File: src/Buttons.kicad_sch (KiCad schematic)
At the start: 23 parts

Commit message: Update Schematics design
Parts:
- renumbered JP4 to JP1, JP5 to JP2, JP6 to JP3
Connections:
- net +BATT: now also SW?.1 (A); no longer SW?.3 (C)
- net GND: now also SW?.3 (C); no longer SW?.1 (A)
- net GND1 renamed GNDDash
- net GND2 renamed GNDEBlinker

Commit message: update Schematics
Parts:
- removed D? (x2): LED, LED_THT:LED_D5.0mm, symbol Device:LED
- removed J? (x4): MiniFit_2x03_F, Connector_Molex:Molex_Mini-Fit_Jr_5566-06A_2x03_P4.20mm_Vertical, symbol Connector_Generic:Conn_02x03_Counter_Clockwise
- removed JP1, JP2, JP3: Jumper_3_Bridged12, symbol Jumper:Jumper_3_Bridged12
- removed R? (x2): 470R, Resistor_THT:R_Axial_DIN0204_L3.6mm_D1.6mm_P5.08mm_Horizontal, symbol Device:R
- removed SW? (x2): SW_SPDT, symbol Switch:SW_SPDT
- added D?: LED, LED_THT:LED_D5.0mm, symbol Device:LED
- added J? (x3): MiniFit_2x03_F, Connector_Molex:Molex_Mini-Fit_Jr_5566-06A_2x03_P4.20mm_Vertical, symbol Connector_Generic:Conn_02x03_Counter_Clockwise
- added JP1: Jumper_3_Open, symbol Jumper:Jumper_3_Open
- added R?: 470R, Resistor_THT:R_Axial_DIN0204_L3.6mm_D1.6mm_P5.08mm_Horizontal, symbol Device:R
- added SW?: SW_SPDT, symbol Switch:SW_SPDT
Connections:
- net +5V: now also J?.3 (Pin_3), JP1.3 (B)
- net +BATT: now also J?.1 (Pin_1), R?.2
- net Accessory: now also R?.2, J?.1 (Pin_1), J?.4 (Pin_4)
- net GND: now also J?.2 (Pin_2), J?.2 (Pin_2), J?.2 (Pin_2), SW?.1 (A)
- net GNDDash: now also D?.1 (K), J?.5 (Pin_5), J?.5 (Pin_5), J?.5 (Pin_5)
- net VInst: now also J?.1 (Pin_1), J?.1 (Pin_1), J?.6 (Pin_6), JP1.1 (A), R?.2; no longer J?.1 (Pin_1), R?.2, R?.2
- net VLight: now also SW?.3 (C), J?.3 (Pin_3)
- net at SW?.3 (C): now also JP1.2 (C)
- net AuxSwitch1 renamed AuxSwitch
- net AuxSwitch: now also J?.4 (Pin_4)
- net BSignal renamed SignalRelay
- net EBlinker renamed Hazard
- net GNDEBlinker renamed HazardLed
- new net: D?.2 (A), R?.1
- new net VOutlet: J?.3 (Pin_3), SW?.3 (C)
- new net VOutlet_Jack: J?.4 (Pin_4), SW?.2 (B)
- no-connect marks 2 -> 3
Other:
- note added: "Auxiliary Beams Buttons"
- note added: "DC Outlet Button"
- note removed: "Auxiliary Beam Buttons"
- note removed: "Kill switch button"
- moved on the sheet: D?, R?, SW?

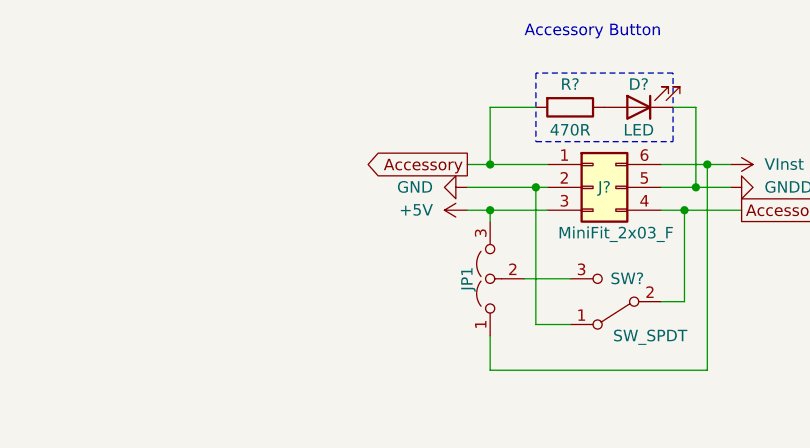
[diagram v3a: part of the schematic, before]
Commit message: Update Schmatics; Cleanup unecessary circuits; Simplify blinkers dimmers; Update PCB; Colorize motorcycle electric diagram.
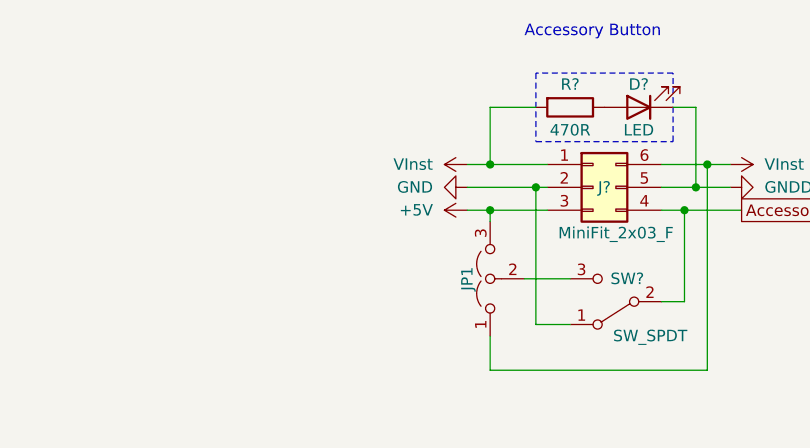
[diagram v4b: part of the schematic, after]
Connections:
- net Accessory: no longer J?.1 (Pin_1), R?.2
- net VInst: now also J?.1 (Pin_1), R?.2
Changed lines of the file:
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@@
-    )
-  )
-  (global_label "Accessory" (shape output) (at 189.23 52.07 180) (fields_autoplaced)
-    (effects (font (size 1.27 1.27)) (justify right))
-    (property "Intersheetrefs" "${INTERSHEET_REFS}" (at 177.0108 52.07 0)
-      (effects (font (size 1.27 1.27)) (justify right) hide)
     )
   )
@@
         )
         (path "/e63e39d7-6ac0-4ffd-8aa3-1841a4541b55/d73eba3b-b563-44cf-9a80-01658b690b2a"
-          (reference "J5") (unit 1)
+          (reference "J42") (unit 1)
         )
       )
@@
         )
         (path "/e63e39d7-6ac0-4ffd-8aa3-1841a4541b55/d73eba3b-b563-44cf-9a80-01658b690b2a"
-          (reference "#PWR045") (unit 1)
+          (reference "#PWR060") (unit 1)
         )
       )
@@
         )
         (path "/e63e39d7-6ac0-4ffd-8aa3-1841a4541b55/d73eba3b-b563-44cf-9a80-01658b690b2a"
-          (reference "D14") (unit 1)
+          (reference "D16") (unit 1)
         )
       )
@@
         )
         (path "/e63e39d7-6ac0-4ffd-8aa3-1841a4541b55/d73eba3b-b563-44cf-9a80-01658b690b2a"
-          (reference "#PWR050") (unit 1)
+          (reference "#PWR062") (unit 1)
         )
       )
@@
         )
         (path "/e63e39d7-6ac0-4ffd-8aa3-1841a4541b55/d73eba3b-b563-44cf-9a80-01658b690b2a"
-          (reference "#PWR040") (unit 1)
+          (reference "#PWR058") (unit 1)
         )
       )
@@
         )
         (path "/e63e39d7-6ac0-4ffd-8aa3-1841a4541b55/d73eba3b-b563-44cf-9a80-01658b690b2a"
-          (reference "J7") (unit 1)
+          (reference "J41") (unit 1)
         )
       )
@@
         )
         (path "/e63e39d7-6ac0-4ffd-8aa3-1841a4541b55/d73eba3b-b563-44cf-9a80-01658b690b2a"
-          (reference "J4") (unit 1)
+          (reference "J43") (unit 1)
+        )
+      )
+    )
+  )
+  (symbol (lib_name "VInst_2") (lib_id "Local Components:VInst") (at 189.23 52.07 90) (unit 1)
+    (in_bom yes) (on_board yes) (dnp no)
+    (property "Reference" "#PWR?" (at 189.23 48.26 0)
+      (effects (font (size 1.27 1.27)) hide)
+    )
+    (property "Value" "VInst" (at 185.42 52.07 90)
+      (effects (font (size 1.27 1.27)) (justify left))
+    )
+    (property "Footprint" "" (at 189.23 52.07 0)
+      (effects (font (size 1.27 1.27)) hide)
+    )
+    (property "Datasheet" "" (at 189.23 52.07 0)
+      (effects (font (size 1.27 1.27)) hide)
+    )
+    (pin "1")
+    (instances
+      (project "dragstar-infotainment"
+        (path "/e63e39d7-6ac0-4ffd-8aa3-1841a4541b55"
+          (reference "#PWR?") (unit 1)
+        )
+        (path "/e63e39d7-6ac0-4ffd-8aa3-1841a4541b55/d73eba3b-b563-44cf-9a80-01658b690b2a"
+          (reference "#PWR057") (unit 1)
         )
       )
@@
         )
         (path "/e63e39d7-6ac0-4ffd-8aa3-1841a4541b55/d73eba3b-b563-44cf-9a80-01658b690b2a"
-          (reference "J6") (unit 1)
+          (reference "J44") (unit 1)
         )
       )
@@
         )
         (path "/e63e39d7-6ac0-4ffd-8aa3-1841a4541b55/d73eba3b-b563-44cf-9a80-01658b690b2a"
-          (reference "#PWR046") (unit 1)
+          (reference "#PWR061") (unit 1)
         )
       )
@@
         )
         (path "/e63e39d7-6ac0-4ffd-8aa3-1841a4541b55/d73eba3b-b563-44cf-9a80-01658b690b2a"
-          (reference "SW1") (unit 1)
+          (reference "SW3") (unit 1)
         )
       )
@@
         )
         (path "/e63e39d7-6ac0-4ffd-8aa3-1841a4541b55/d73eba3b-b563-44cf-9a80-01658b690b2a"
-          (reference "#PWR041") (unit 1)
+          (reference "#PWR065") (unit 1)
         )
       )
@@
         )
         (path "/e63e39d7-6ac0-4ffd-8aa3-1841a4541b55/d73eba3b-b563-44cf-9a80-01658b690b2a"
-          (reference "#PWR053") (unit 1)
+          (reference "#PWR056") (unit 1)
         )
       )
@@
         )
         (path "/e63e39d7-6ac0-4ffd-8aa3-1841a4541b55/d73eba3b-b563-44cf-9a80-01658b690b2a"
-          (reference "#PWR044") (unit 1)
+          (reference "#PWR054") (unit 1)
         )
       )
@@
         )
         (path "/e63e39d7-6ac0-4ffd-8aa3-1841a4541b55/d73eba3b-b563-44cf-9a80-01658b690b2a"
-          (reference "D16") (unit 1)
+          (reference "D15") (unit 1)
         )
       )
@@
         )
         (path "/e63e39d7-6ac0-4ffd-8aa3-1841a4541b55/d73eba3b-b563-44cf-9a80-01658b690b2a"
-          (reference "R7") (unit 1)
+          (reference "R11") (unit 1)
         )
       )
@@
         )
         (path "/e63e39d7-6ac0-4ffd-8aa3-1841a4541b55/d73eba3b-b563-44cf-9a80-01658b690b2a"
-          (reference "#PWR049") (unit 1)
+          (reference "#PWR055") (unit 1)
         )
       )
@@
         )
         (path "/e63e39d7-6ac0-4ffd-8aa3-1841a4541b55/d73eba3b-b563-44cf-9a80-01658b690b2a"
-          (reference "R8") (unit 1)
+          (reference "R10") (unit 1)
         )
       )
@@
         )
         (path "/e63e39d7-6ac0-4ffd-8aa3-1841a4541b55/d73eba3b-b563-44cf-9a80-01658b690b2a"
-          (reference "D15") (unit 1)
+          (reference "D18") (unit 1)
         )
       )
@@
         )
         (path "/e63e39d7-6ac0-4ffd-8aa3-1841a4541b55/d73eba3b-b563-44cf-9a80-01658b690b2a"
-          (reference "#PWR039") (unit 1)
+          (reference "#PWR064") (unit 1)
         )
       )
@@
         )
         (path "/e63e39d7-6ac0-4ffd-8aa3-1841a4541b55/d73eba3b-b563-44cf-9a80-01658b690b2a"
-          (reference "#PWR047") (unit 1)
+          (reference "#PWR063") (unit 1)
         )
       )
@@
         )
         (path "/e63e39d7-6ac0-4ffd-8aa3-1841a4541b55/d73eba3b-b563-44cf-9a80-01658b690b2a"
-          (reference "R9") (unit 1)
+          (reference "R12") (unit 1)
         )
       )
@@
         )
         (path "/e63e39d7-6ac0-4ffd-8aa3-1841a4541b55/d73eba3b-b563-44cf-9a80-01658b690b2a"
-          (reference "D13") (unit 1)
+          (reference "D17") (unit 1)
         )
       )
@@
         )
         (path "/e63e39d7-6ac0-4ffd-8aa3-1841a4541b55/d73eba3b-b563-44cf-9a80-01658b690b2a"
-          (reference "#PWR042") (unit 1)
+          (reference "#PWR059") (unit 1)
         )
       )
@@
         )
         (path "/e63e39d7-6ac0-4ffd-8aa3-1841a4541b55/d73eba3b-b563-44cf-9a80-01658b690b2a"
-          (reference "#PWR048") (unit 1)
+          (reference "#PWR050") (unit 1)
         )
       )
@@
         )
         (path "/e63e39d7-6ac0-4ffd-8aa3-1841a4541b55/5d40715c-dfc9-4b95-9cc7-adbd4b609d9b"
-          (reference "#PWR027") (unit 1)
+          (reference "#PWR?") (unit 1)
         )
         (path "/e63e39d7-6ac0-4ffd-8aa3-1841a4541b55/5d40715c-dfc9-4b95-9cc7-adbd4b609d9b/cd89aa2b-c893-42fb-9925-ff5352d2269d"
-          (reference "#PWR0105") (unit 1)
-        )
-        (path "/e63e39d7-6ac0-4ffd-8aa3-1841a4541b55/d73eba3b-b563-44cf-9a80-01658b690b2a"
-          (reference "#PWR038") (unit 1)
+          (reference "#PWR?") (unit 1)
+        )
+        (path "/e63e39d7-6ac0-4ffd-8aa3-1841a4541b55/d73eba3b-b563-44cf-9a80-01658b690b2a"
+          (reference "#PWR053") (unit 1)
         )
       )
@@
         )
         (path "/e63e39d7-6ac0-4ffd-8aa3-1841a4541b55/d73eba3b-b563-44cf-9a80-01658b690b2a"
-          (reference "SW3") (unit 1)
+          (reference "SW4") (unit 1)
         )
       )
@@
         )
         (path "/e63e39d7-6ac0-4ffd-8aa3-1841a4541b55/d73eba3b-b563-44cf-9a80-01658b690b2a"
-          (reference "R10") (unit 1)
+          (reference "R9") (unit 1)
         )
       )
@@
         )
         (path "/e63e39d7-6ac0-4ffd-8aa3-1841a4541b55/d73eba3b-b563-44cf-9a80-01658b690b2a"
-          (reference "SW4") (unit 1)
-        )
-      )
+          (reference "SW1") (unit 1)
+        )
+      )

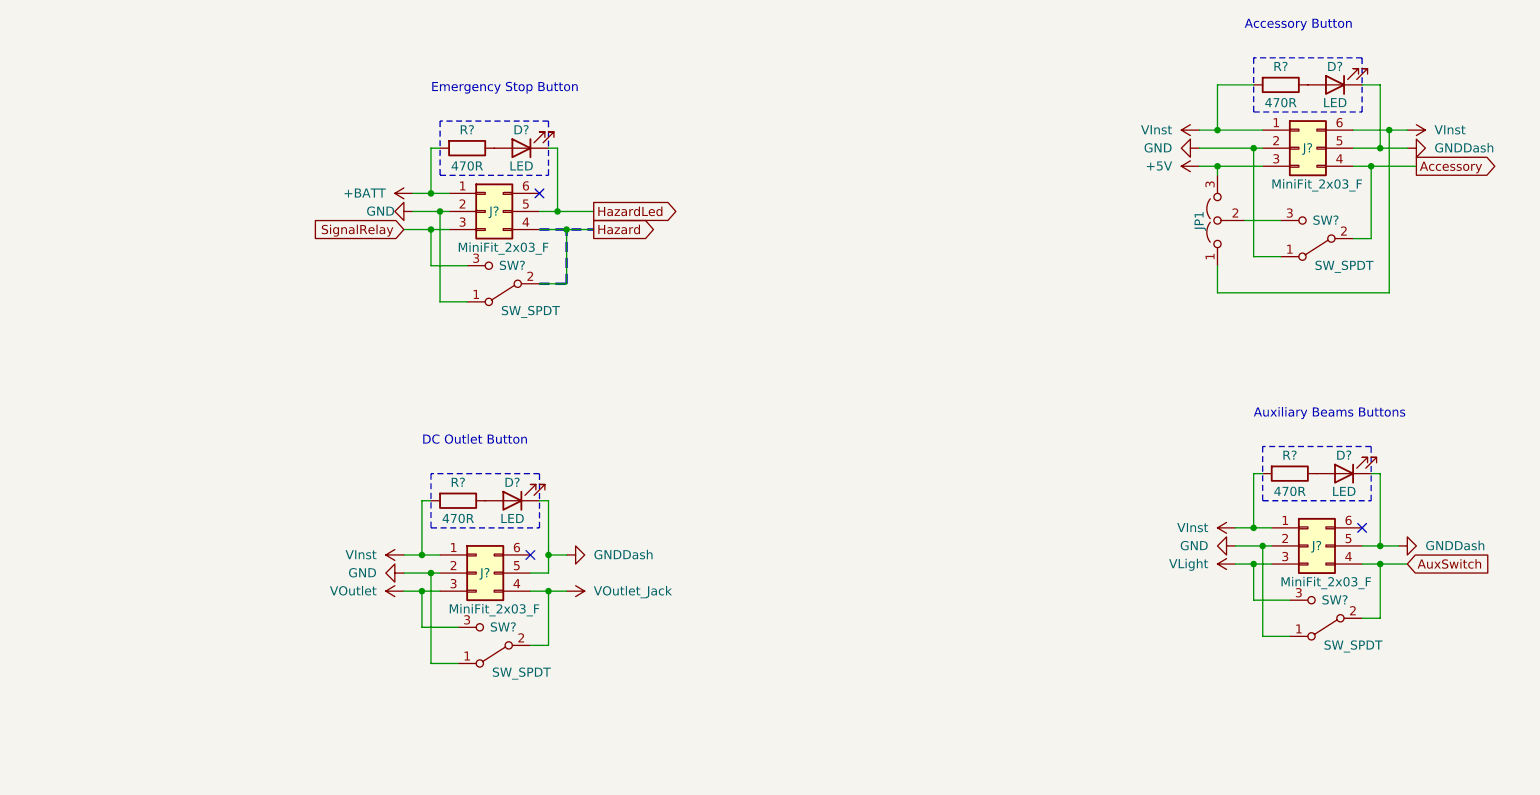
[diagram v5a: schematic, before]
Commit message: simplify circuit diagram. Remove unecessary features; Split board into two components|
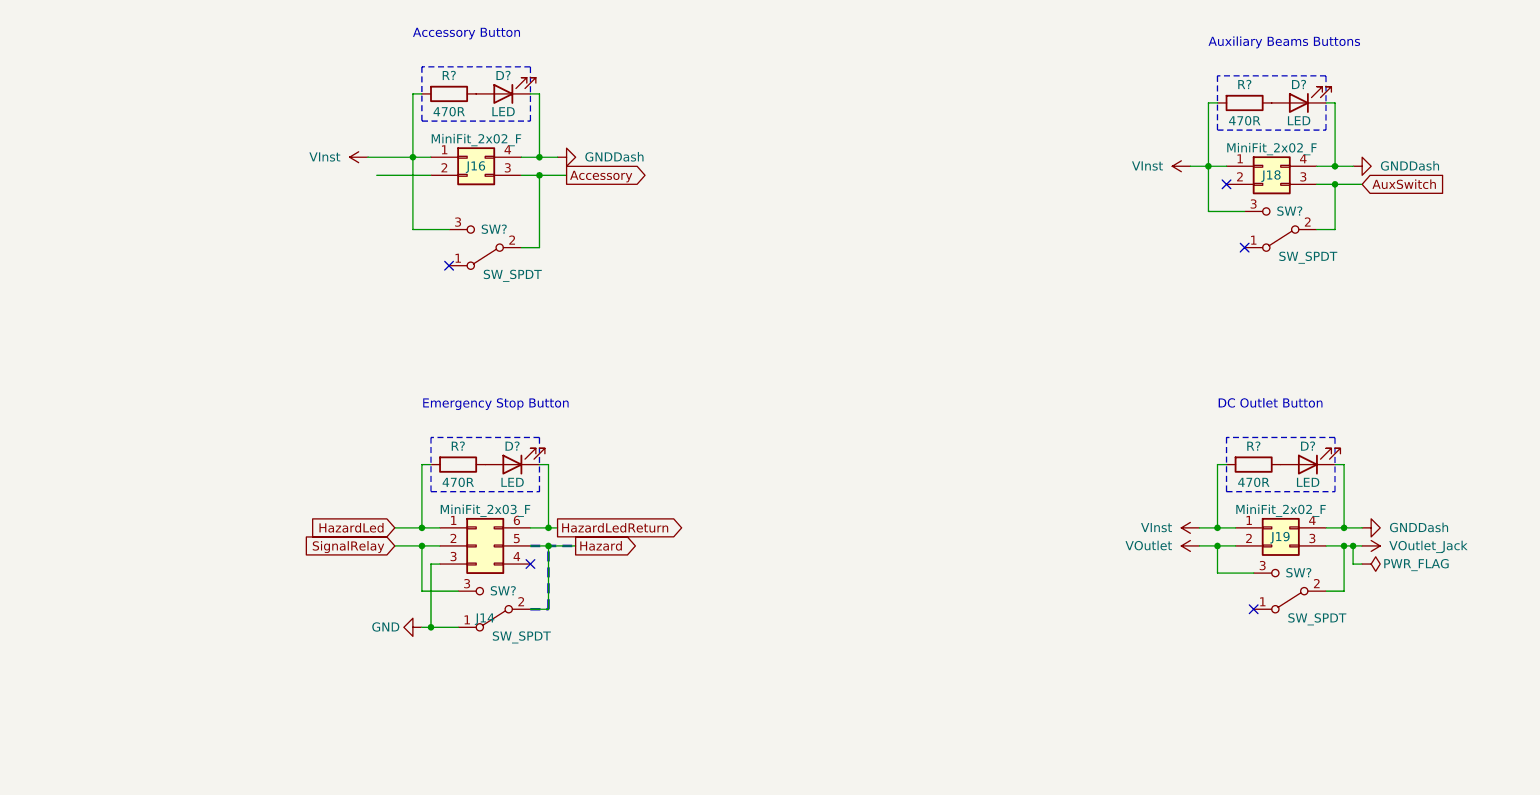
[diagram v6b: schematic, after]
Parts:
- removed J? (x4): MiniFit_2x03_F, Connector_Molex:Molex_Mini-Fit_Jr_5566-06A_2x03_P4.20mm_Vertical, symbol Connector_Generic:Conn_02x03_Counter_Clockwise
- removed JP1: Jumper_3_Open, symbol Jumper:Jumper_3_Open
- added J14: MiniFit_2x03_F, symbol Connector_Generic:Conn_02x03_Counter_Clockwise
- added J16, J18, J19: MiniFit_2x02_F, symbol Connector_Generic:Conn_02x02_Counter_Clockwise
- D? (x4): footprint LED_THT:LED_D5.0mm -> (none)
- R? (x4): footprint Resistor_THT:R_Axial_DIN0204_L3.6mm_D1.6mm_P5.08mm_Horizontal -> (none)
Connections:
- net +BATT is gone; now on net HazardLed: R?.2
- net VLight is gone; now on net VInst: SW?.3 (C)
- net Accessory: now also J16.3 (Pin_3)
- net AuxSwitch: now also J18.3 (Pin_3)
- net GND: now also J14.3 (Pin_3); no longer SW?.1 (A), SW?.1 (A), SW?.1 (A)
- net GNDDash: now also J16.4 (Pin_4), J18.4 (Pin_4), J19.4 (Pin_4)
- net Hazard: now also J14.5 (Pin_5)
- net HazardLed: now also J14.1 (Pin_1); no longer D?.1 (K)
- net SignalRelay: now also J14.2 (Pin_2)
- net VInst: now also SW?.3 (C), J16.1 (Pin_1), J18.1 (Pin_1), J19.1 (Pin_1)
- net VOutlet: now also J19.2 (Pin_2)
- net VOutlet_Jack: now also J19.3 (Pin_3)
- new net HazardLedReturn: D?.1 (K), J14.6 (Pin_6)
- no-connect marks 3 -> 5
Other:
- moved on the sheet: D?, R?, SW?
